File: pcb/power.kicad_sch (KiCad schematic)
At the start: 40 parts, among them J1 XT30PW-M, Q1 NTR4003N, Q2 NTR4003N, Q3 Si3407DV, SW3 SLW-864574-5A-RA-N-D, U2 TPS561246DRLR, U3 ZXCT180A4W5

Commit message: Add MPN field for components except resistors
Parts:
- C16, C22: MPN (none) -> CL21A226MAYNNNE
- C17, C19, C20, C23: MPN (none) -> CL10B104KB8NNWC
- C18: MPN (none) -> CL10B105MO8NNWC
- C21: MPN (none) -> CL10C100JB8NNNC
- D1: MPN (none) -> SS12
- J1: MPN (none) -> XT30PW-M
- L1: MPN (none) -> AMPI0640ED2R2MT
- Q1, Q2: MPN (none) -> NTR4003N
- Q3: MPN (none) -> Si3407DV
- SW3: MPN (none) -> SLW-864574-5A-RA-N-D
- TP1, TP10, TP11, TP2, TP3, TP4, TP5, TP6, TP7, TP8, TP9: MPN (none) -> RCUCTE
- U2: MPN (none) -> TPS561246DRLR
- U3: MPN (none) -> ZXCT180A4W5

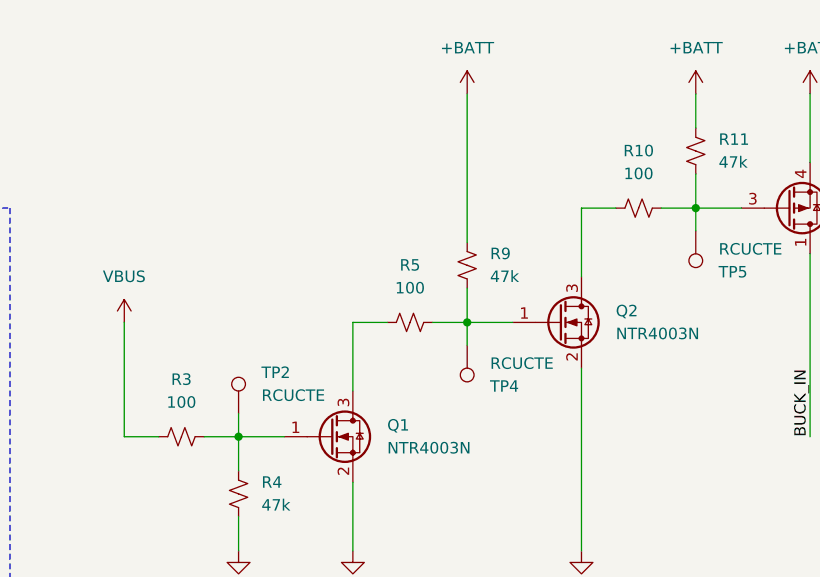
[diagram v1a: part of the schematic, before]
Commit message: BOM optimize 100 ohm resistors to 150 ohm
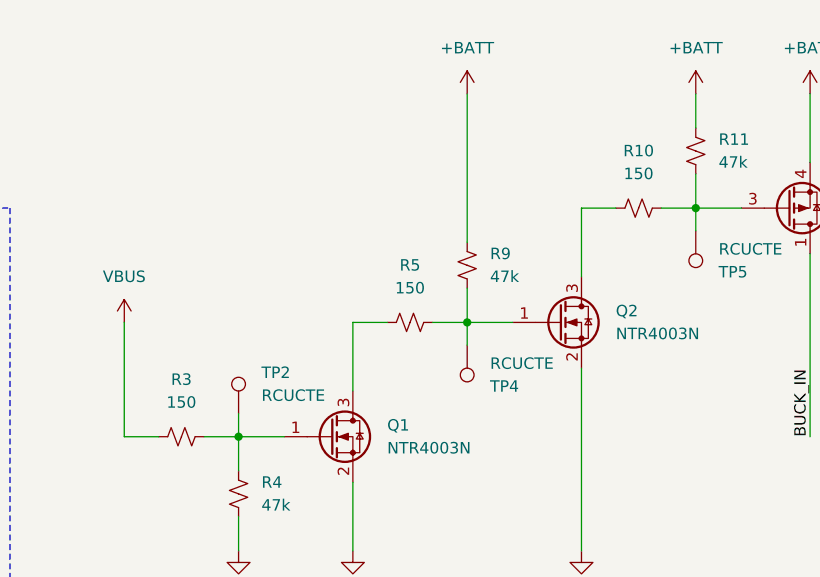
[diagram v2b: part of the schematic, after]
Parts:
- R10, R3, R5: value 100 -> 150
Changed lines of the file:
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@@
 			)
 		)
-		(property "Value" "100"
+		(property "Value" "150"
 			(at 107.95 85.09 90)
 			(effects
@@
 			)
 		)
-		(property "Value" "100"
+		(property "Value" "150"
 			(at 82.55 97.79 90)
 			(effects
@@
 			)
 		)
-		(property "Value" "100"
+		(property "Value" "150"
 			(at 57.15 110.49 90)
 			(effects

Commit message: BOM optimize VBUS LED
600R to 3x 150R = 450R for 6.667 mA
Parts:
- R14: MPN (none) -> PA0805FRE7W0R002L
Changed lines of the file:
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@@
 			)
 		)
-		(property "MPN" ""
+		(property "MPN" "PA0805FRE7W0R002L"
 			(at 165.1 44.45 0)
 			(effects

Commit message: Update resistor MPNs
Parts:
- R10, R3, R5: MPN (none) -> RC0603JR-07150RL
- R11, R4, R6, R8, R9: MPN (none) -> RC0603FR-0747KL
- R12: MPN (none) -> RT0603BRD07135KL
- R13: MPN (none) -> AC0603FR-0730KL
- R7: MPN (none) -> RC0603FR-0782KL
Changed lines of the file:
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@@
 			)
 		)
-		(property "MPN" ""
+		(property "MPN" "RC0603FR-0747KL"
 			(at 114.3 82.55 0)
 			(effects
@@
 			)
 		)
-		(property "MPN" ""
+		(property "MPN" "RT0603BRD07135KL"
 			(at 139.7 158.75 0)
 			(effects
@@
 			)
 		)
-		(property "MPN" ""
+		(property "MPN" "RC0603FR-0782KL"
 			(at 88.9 31.75 0)
 			(effects
@@
 			)
 		)
-		(property "MPN" ""
+		(property "MPN" "RC0603FR-0747KL"
 			(at 88.9 44.45 0)
 			(effects
@@
 			)
 		)
-		(property "MPN" ""
+		(property "MPN" "RC0603JR-07150RL"
 			(at 107.95 88.9 90)
 			(effects
@@
 			)
 		)
-		(property "MPN" ""
+		(property "MPN" "AC0603FR-0730KL"
 			(at 139.7 171.45 0)
 			(effects
@@
 			)
 		)
-		(property "MPN" ""
+		(property "MPN" "RC0603FR-0747KL"
 			(at 82.55 158.75 0)
 			(effects
@@
 			)
 		)
-		(property "MPN" ""
+		(property "MPN" "RC0603JR-07150RL"
 			(at 82.55 101.6 90)
 			(effects
@@
 			)
 		)
-		(property "MPN" ""
+		(property "MPN" "RC0603FR-0747KL"
 			(at 63.5 120.65 0)
 			(effects
@@
 			)
 		)
-		(property "MPN" ""
+		(property "MPN" "RC0603FR-0747KL"
 			(at 88.9 95.25 0)
 			(effects
@@
 			)
 		)
-		(property "MPN" ""
+		(property "MPN" "RC0603JR-07150RL"
 			(at 57.15 114.3 90)
 			(effects

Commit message: Update MPNs to optimize for HQ Online
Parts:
- C18: MPN CL10B105MO8NNWC -> CL10A105KA8NNNC
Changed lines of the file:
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@@
 			)
 		)
-		(property "MPN" "CL10B105MO8NNWC"
+		(property "MPN" "CL10A105KA8NNNC"
 			(at 82.55 171.45 0)
 			(effects

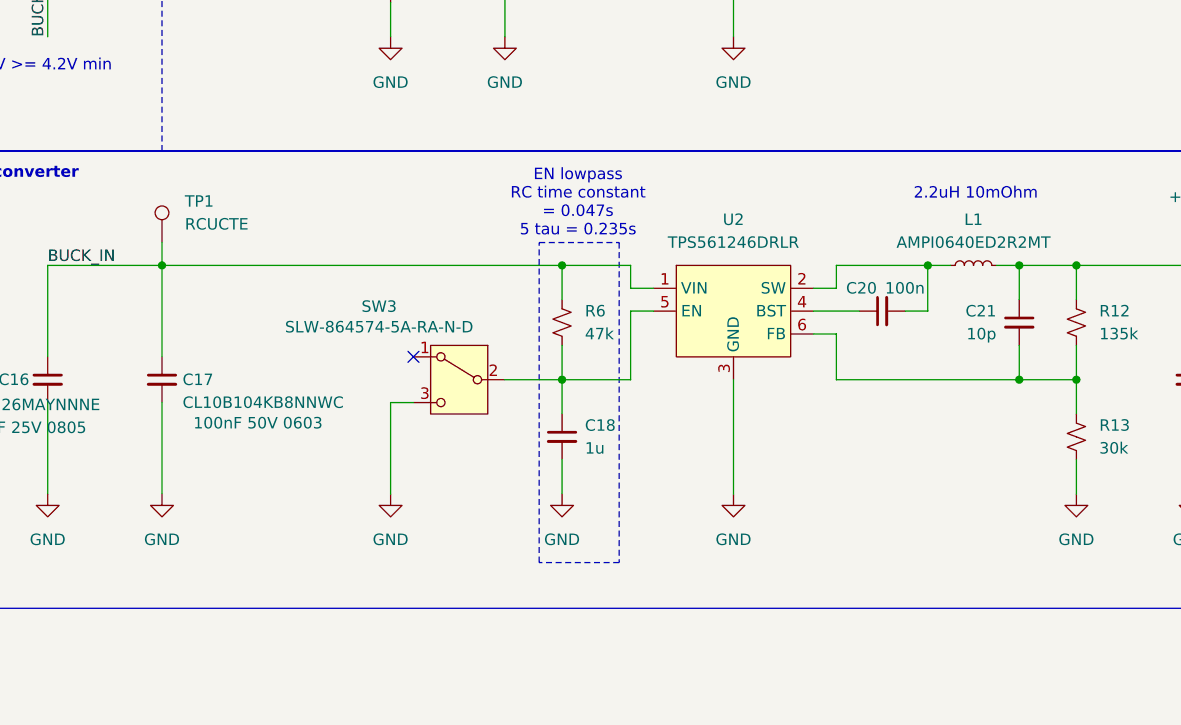
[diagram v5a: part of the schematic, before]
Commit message: Fix buck EN
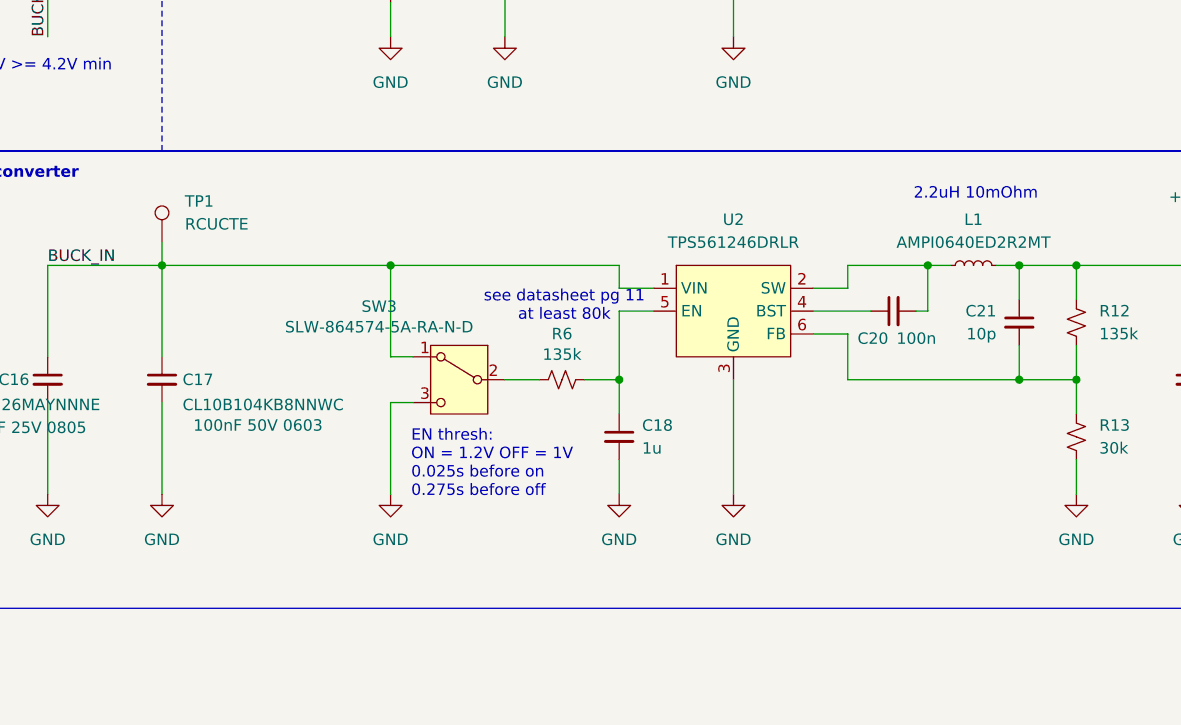
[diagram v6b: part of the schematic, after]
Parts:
- R6: value 47k -> 135k
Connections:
- net BUCK_IN: now also SW3.1 (A); no longer R6.1
- net at C18.1, R6.2, U2.5 (EN): no longer SW3.2 (B)
- new net: R6.1, SW3.2 (B)
- no-connect marks 1 -> 0
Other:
- note added: "EN thresh: ON = 1.2V OFF = 1V 0.025s before on 0.275s before off"
- note added: "see datasheet pg 11 at least 80k"
- note removed: "EN lowpass RC time constant = 0.047s 5 tau = 0.235s"
- moved on the sheet: C18, C20, R6

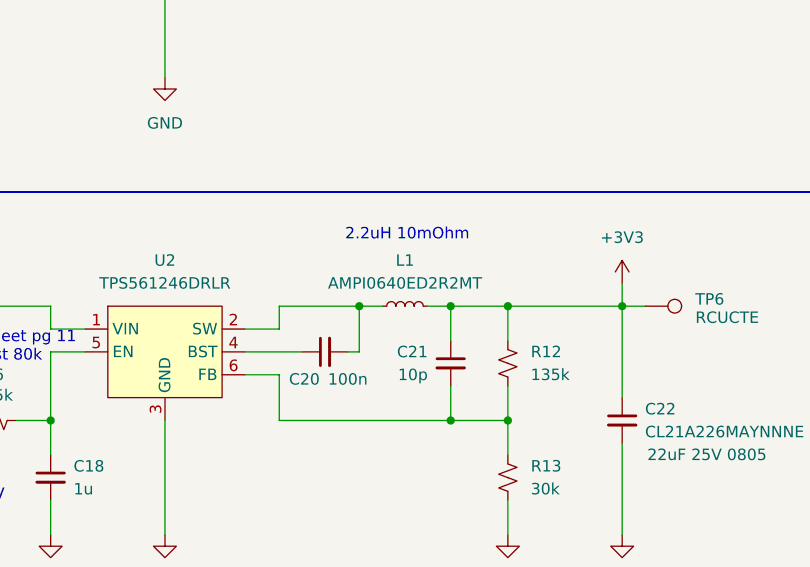
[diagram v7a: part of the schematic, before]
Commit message: Replace inductor with HQOnline alternative
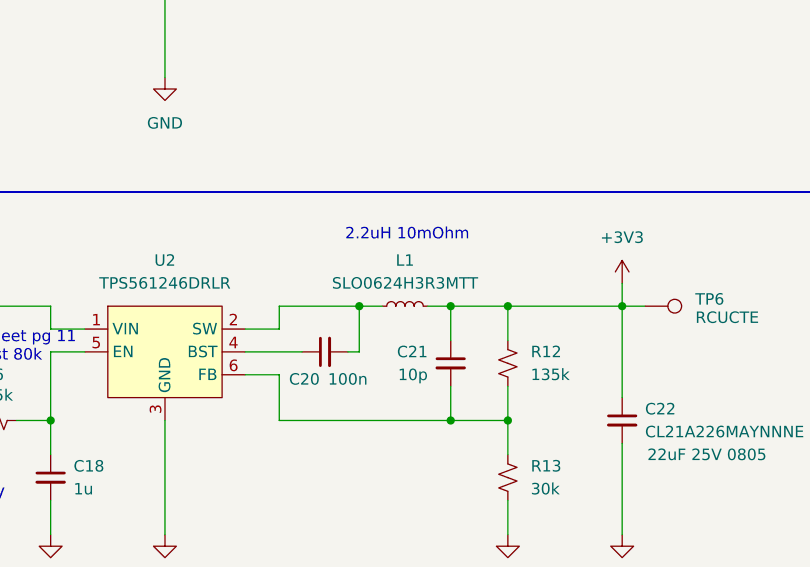
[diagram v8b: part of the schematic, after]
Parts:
- L1: value AMPI0640ED2R2MT -> SLO0624H3R3MTT; footprint L_Arlitech:L_Arlitech_AMPI0640ED2R2MT_6.6mm_7.1mm_2628_6671_Metric -> L_Sunltech:L_Sunltech_SLO0624H; MPN AMPI0640ED2R2MT -> SLO0624H3R3MTT
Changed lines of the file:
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@@
 			)
 		)
-		(property "Value" "AMPI0640ED2R2MT"
+		(property "Value" "SLO0624H3R3MTT"
 			(at 128.27 149.86 90)
 			(effects
@@
 			)
 		)
-		(property "Footprint" "L_Arlitech:L_Arlitech_AMPI0640ED2R2MT_6.6mm_7.1mm_2628_6671_Metric"
+		(property "Footprint" "L_Sunltech:L_Sunltech_SLO0624H"
 			(at 128.27 152.4 0)
 			(effects
@@
 			)
 		)
-		(property "Datasheet" "~"
+		(property "Datasheet" "https://file.elecfans.com/web2/M00/42/8B/pYYBAGJ5AK-AFbIwAA3vuOUpZHE121.pdf"
 			(at 128.27 152.4 0)
 			(effects
@@
 			)
 		)
-		(property "MPN" "AMPI0640ED2R2MT"
+		(property "MPN" "SLO0624H3R3MTT"
 			(at 128.27 152.4 90)
 			(effects
